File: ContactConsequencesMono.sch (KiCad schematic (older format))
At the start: 7 parts

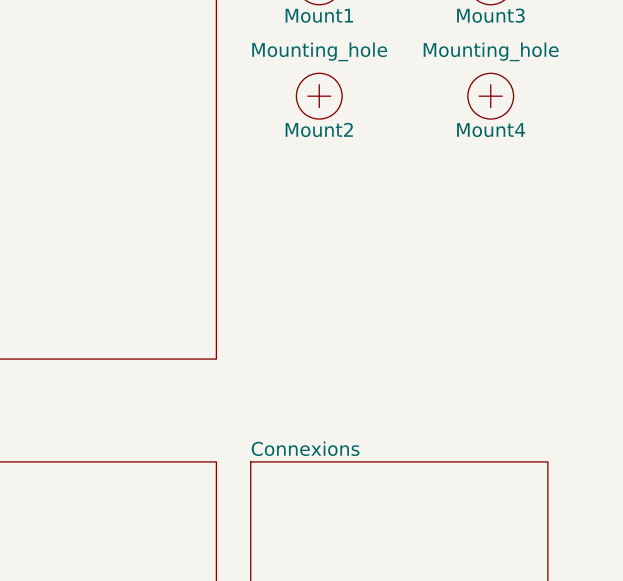
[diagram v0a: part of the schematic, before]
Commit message: Board modified after ckecking. Ready for fab, just need to create gerber, position and components files.
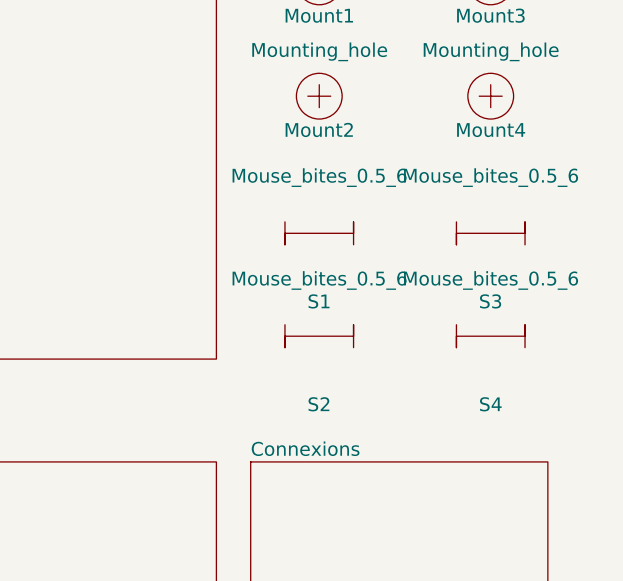
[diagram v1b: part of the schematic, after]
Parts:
- added S1, S2, S3, S4: Mouse_bites_0.5_6, Holes_Fids:Mouse_bites_0.5_6, symbol Mouse_bites_0.5_6
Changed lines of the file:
@@
 EESchema Schematic File Version 2
+LIBS:ContactConsequencesMono-rescue
 LIBS:switches-perso
 LIBS:Logos
@@
 	1    0    0    -1
 $EndComp
+$Comp
+L Mouse_bites_0.5_6 S1
+U 1 1 59CDD6D3
+P 9800 2950
+F 0 "S1" H 9800 2650 60  0000 C CNN
+F 1 "Mouse_bites_0.5_6" H 9800 3200 60  0000 C CNN
+F 2 "Holes_Fids:Mouse_bites_0.5_6" H 9800 2950 60  0001 C CNN
+F 3 "" H 9800 2950 60  0001 C CNN
+	1    9800 2950
+	1    0    0    -1
+$EndComp
+$Comp
+L Mouse_bites_0.5_6 S3
+U 1 1 59CDD752
+P 10550 2950
+F 0 "S3" H 10550 2650 60  0000 C CNN
+F 1 "Mouse_bites_0.5_6" H 10550 3200 60  0000 C CNN
+F 2 "Holes_Fids:Mouse_bites_0.5_6" H 10550 2950 60  0001 C CNN
+F 3 "" H 10550 2950 60  0001 C CNN
+	1    10550 2950
+	1    0    0    -1
+$EndComp
+$Comp
+L Mouse_bites_0.5_6 S2
+U 1 1 59CDD797
+P 9800 3400
+F 0 "S2" H 9800 3100 60  0000 C CNN
+F 1 "Mouse_bites_0.5_6" H 9800 3650 60  0000 C CNN
+F 2 "Holes_Fids:Mouse_bites_0.5_6" H 9800 3400 60  0001 C CNN
+F 3 "" H 9800 3400 60  0001 C CNN
+	1    9800 3400
+	1    0    0    -1
+$EndComp
+$Comp
+L Mouse_bites_0.5_6 S4
+U 1 1 59CDD857
+P 10550 3400
+F 0 "S4" H 10550 3100 60  0000 C CNN
+F 1 "Mouse_bites_0.5_6" H 10550 3650 60  0000 C CNN
+F 2 "Holes_Fids:Mouse_bites_0.5_6" H 10550 3400 60  0001 C CNN
+F 3 "" H 10550 3400 60  0001 C CNN
+	1    10550 3400
+	1    0    0    -1
+$EndComp
